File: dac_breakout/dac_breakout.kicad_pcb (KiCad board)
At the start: 2 copper layers, 57.9 x 29 mm, 24 parts, among them J101 Conn_Coaxial_x2, J102 Conn_02x06_Odd_Even, U101 PCM5102A, U102 AZ1117-3.3

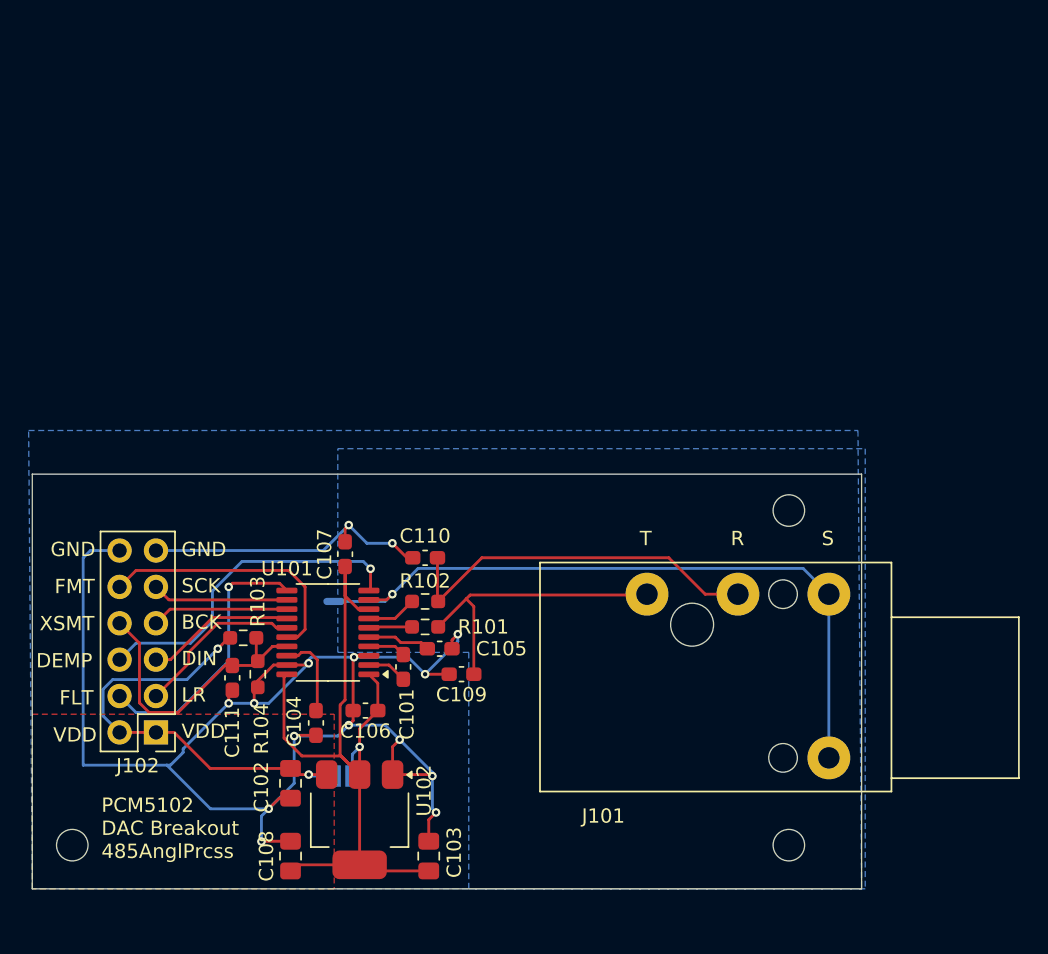
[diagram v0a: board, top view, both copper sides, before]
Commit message: Made breakboard compatible
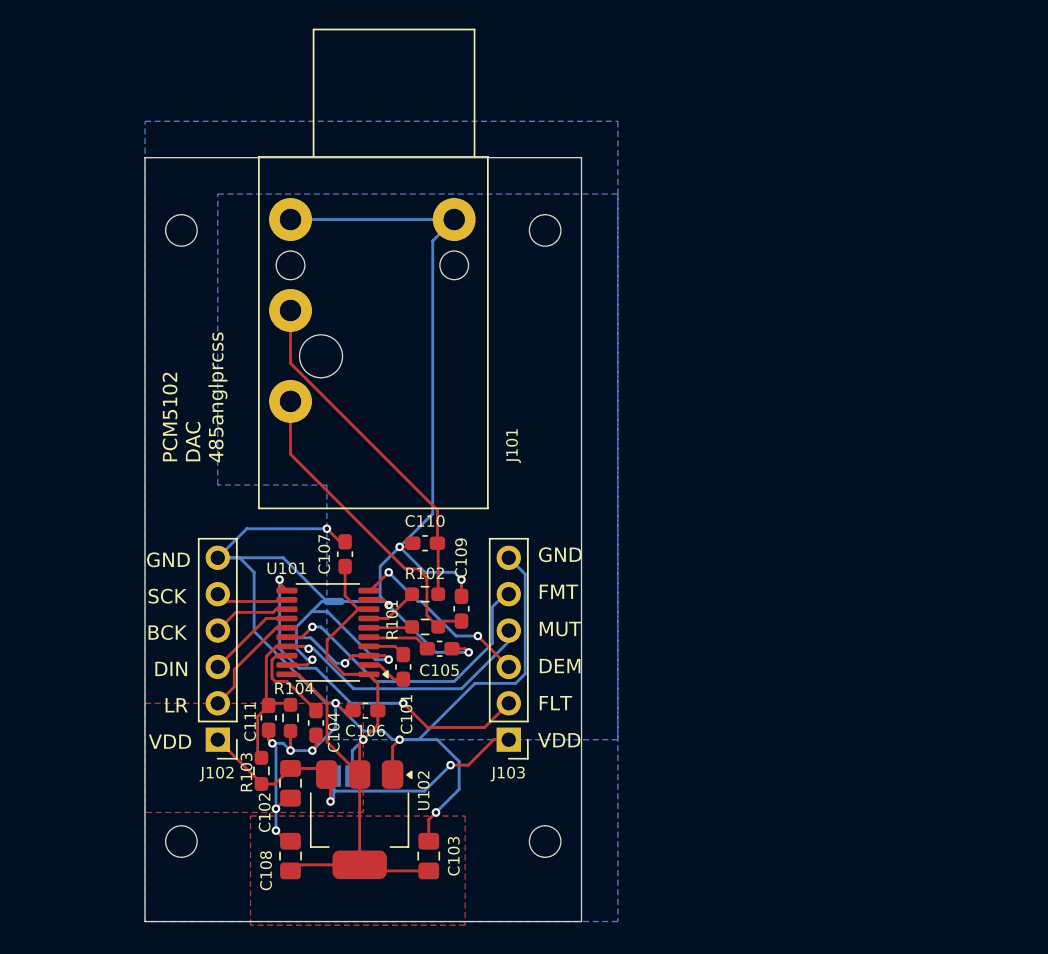
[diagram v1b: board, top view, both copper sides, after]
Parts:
- added J103: Conn_01x06, Connector_PinHeader_2.54mm:PinHeader_1x06_P2.54mm_Vertical, F.Cu at (167.6, 78.7)
- added REF**: MountingHole_2.2mm_M2_DIN965, MountingHole:MountingHole_2.2mm_M2_DIN965, F.Cu at (170.2, 43.2)
- J102: value Conn_02x06_Odd_Even -> Conn_01x06; footprint Connector_PinHeader_2.54mm:PinHeader_2x06_P2.54mm_Vertical -> Connector_PinHeader_2.54mm:PinHeader_1x06_P2.54mm_Vertical
- moved REF** 46.7 mm to (144.8, 43.2)
- moved J101 28.3 mm to (152.4, 55.1), turned to 90 degrees
- moved REF** 17.0 mm to (170.2, 85.9)
- moved R103 9.38 mm to (150.4, 80.9), turned to 90 degrees
- moved REF** 7.62 mm to (144.8, 85.9)
- moved C109 4.57 mm to (164.3, 69.6), turned to 90 degrees
- moved J102 4.35 mm to (147.3, 78.7)
- moved R104 3.81 mm to (152.4, 77.2)
- moved C111 3.78 mm to (150.9, 77.2)
- moved C110 1.02 mm to (161.8, 65.0)
- moved R102 0.51 mm to (161.8, 68.6)
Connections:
- C105 pad 2: GND -> GNDA
- C109 pad 2: GND -> GNDA
- C110 pad 2: GND -> GNDA
- J102 pad 2: VDD -> /LRCK
- J102 pad 3: /LRCK -> /DIN
- J102 pad 4: /FLT -> /BCK
- J102 pad 5: /DIN -> /SCK
- J102 pad 6: /DEMP -> GND
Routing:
- net GND: track 130.6 -> 115.4 mm, vias 15 -> 12
- net GNDA: track 49.0 -> 61.4 mm, vias 1 -> 4
- net /DEMP: track 23.5 -> 13.0 mm, vias 1 -> 2
- net /XSMT: track 20.3 -> 29.7 mm, vias 0 -> 1
- net +3V3: track 56.5 -> 48.3 mm
- net /FLT: track 19.1 -> 24.8 mm, vias 1 -> 2
- net /SCK: track 9.52 -> 5.08 mm
- net /DIN: track 10.4 -> 6.23 mm
- net /LRCK: track 11.8 -> 7.71 mm
- net /BCK: track 9.55 -> 5.44 mm
- net VDD: track 31.3 -> 28.1 mm
- net /FMT: track 18.4 -> 21.4 mm, vias 0 -> 1
- net Net-(J101-IN2): track 26.3 -> 24.1 mm
- net Net-(J101-IN1): track 21.0 -> 22.3 mm
- added copper zone on F.Cu, net +3V3
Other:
- board size 57.9 x 29 mm -> 30.5 x 53.3 mm
- board text added: "DEM"
- board text added: "MUT"
- board text added: "PCM5102 DAC 485anglprcss"
- board text removed: "DEMP"
- board text removed: "PCM5102 DAC Breakout 485AnglPrcss"
- board text removed: "R"
- board text removed: "S"
- board text removed: "T"
- board text removed: "XSMT"
